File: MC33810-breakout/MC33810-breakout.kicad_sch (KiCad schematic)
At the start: 11 parts, among them J1 6473423-1, P1 Pad, P2 Pad, P3 Pad, P4 Pad, U2 XC6206P332MR

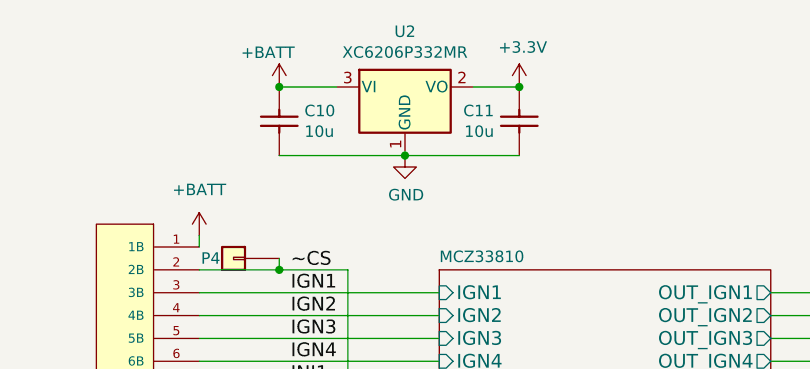
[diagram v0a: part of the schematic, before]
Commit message: Fix LDO
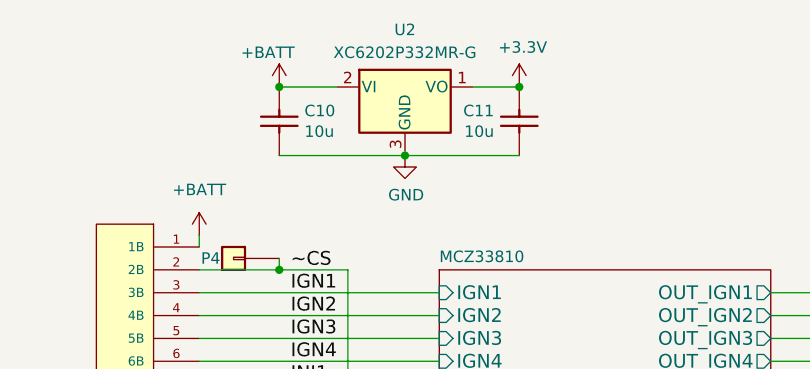
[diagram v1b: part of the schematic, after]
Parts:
- removed U2: XC6206P332MR, Package_TO_SOT_SMD:SOT-23-3, symbol Regulator_Linear:XC6206PxxxMR
- added U2: XC6202P332MR-G, Package_TO_SOT_SMD:SOT-23, symbol Regulator_Linear:LM3480-3.3
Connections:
- net +3.3V: now also U2.1 (VO)
- net +BATT: now also U2.2 (VI)
- net GND: now also U2.3 (GND)
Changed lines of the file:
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@@
     (effects (font (size 1.524 1.524)) (justify left bottom))
+  )
+  (symbol (lib_id "Regulator_Linear:LM3480-3.3") (at 125.73 48.26 0) (unit 1)
+    (in_bom yes) (on_board yes) (dnp no) (fields_autoplaced)
+    (property "Reference" "U2" (at 125.73 41.91 0)
+      (effects (font (size 1.27 1.27)))
+    )
+    (property "Value" "XC6202P332MR-G" (at 125.73 44.45 0)
+      (effects (font (size 1.27 1.27)))
+    )
+    (property "Footprint" "Package_TO_SOT_SMD:SOT-23" (at 125.73 42.545 0)
+      (effects (font (size 1.27 1.27) italic) hide)
+    )
+    (property "Datasheet" "https://datasheet.lcsc.com/lcsc/2304140030_Torex-Semicon-XC6202P332MR-G_C47374.pdf" (at 125.73 48.26 0)
+      (effects (font (size 1.27 1.27)) hide)
+    )
+    (property "LCSC" "C47374" (at 125.73 48.26 0)
+      (effects (font (size 1.524 1.524)) hide)
+    )
+    (pin "1")
+    (pin "2")
+    (pin "3")
+    (instances
+      (project "MC33810-breakout"
+        (path "/03caada9-9e22-4e2d-9035-b15433dfbb17"
+          (reference "U2") (unit 1)
+        )
+      )
+    )
   )
   (symbol (lib_id "rusefi_logo:RUSEFI_LOGO") (at 182.88 171.45 0) (unit 1)
@@
         )
       )
-    )
-  )
-  (symbol (lib_id "Regulator_Linear:XC6206PxxxMR") (at 125.73 48.26 0) (unit 1)
-    (in_bom yes) (on_board yes) (dnp no)
-    (property "Reference" "U2" (at 125.73 42.1132 0)
-      (effects (font (size 1.27 1.27)))
-    )
-    (property "Value" "XC6206P332MR" (at 125.73 44.4246 0)
-      (effects (font (size 1.27 1.27)))
-    )
-    (property "Footprint" "Package_TO_SOT_SMD:SOT-23-3" (at 125.73 42.545 0)
-      (effects (font (size 1.27 1.27) italic) hide)
-    )
-    (property "Datasheet" "https://www.torexsemi.com/file/xc6206/XC6206.pdf" (at 125.73 48.26 0)
-      (effects (font (size 1.27 1.27)) hide)
-    )
-    (property "LCSC" "C5446" (at 125.73 48.26 0)
-      (effects (font (size 1.27 1.27)) hide)
-    )
-    (pin "1")
-    (pin "2")
-    (pin "3")
-    (instances
-      (project "MC33810-breakout"
-        (path "/03caada9-9e22-4e2d-9035-b15433dfbb17"
-          (reference "U2") (unit 1)
-        )
-      )
